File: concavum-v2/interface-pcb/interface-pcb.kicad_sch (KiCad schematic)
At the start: 6 parts, among them J1 Audio_Jack, J2 FPC_connector, U1 Adafruit_KB2040

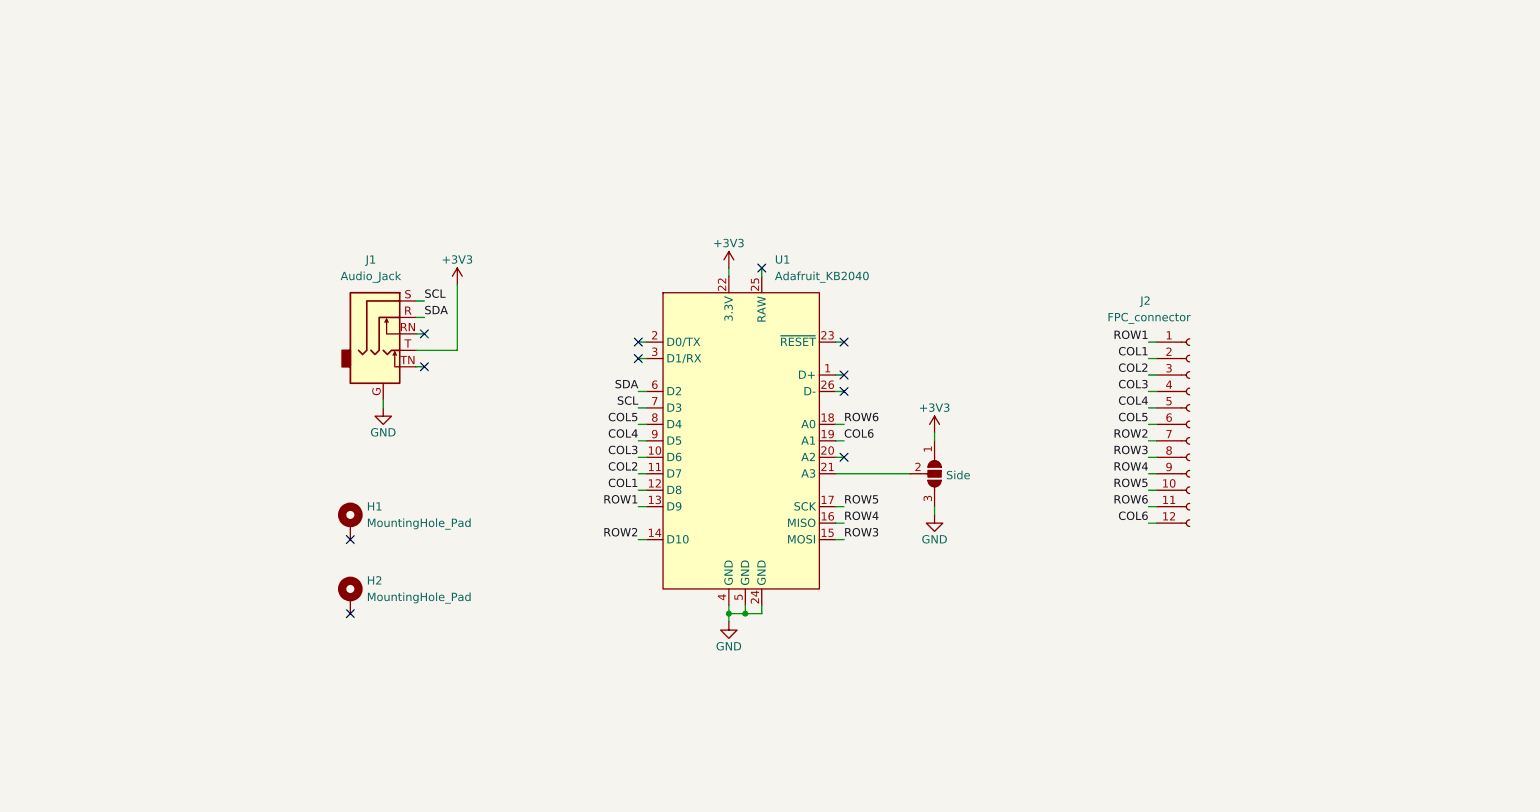
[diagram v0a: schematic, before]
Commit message: Implement VBUS detection and make PCB symmetric
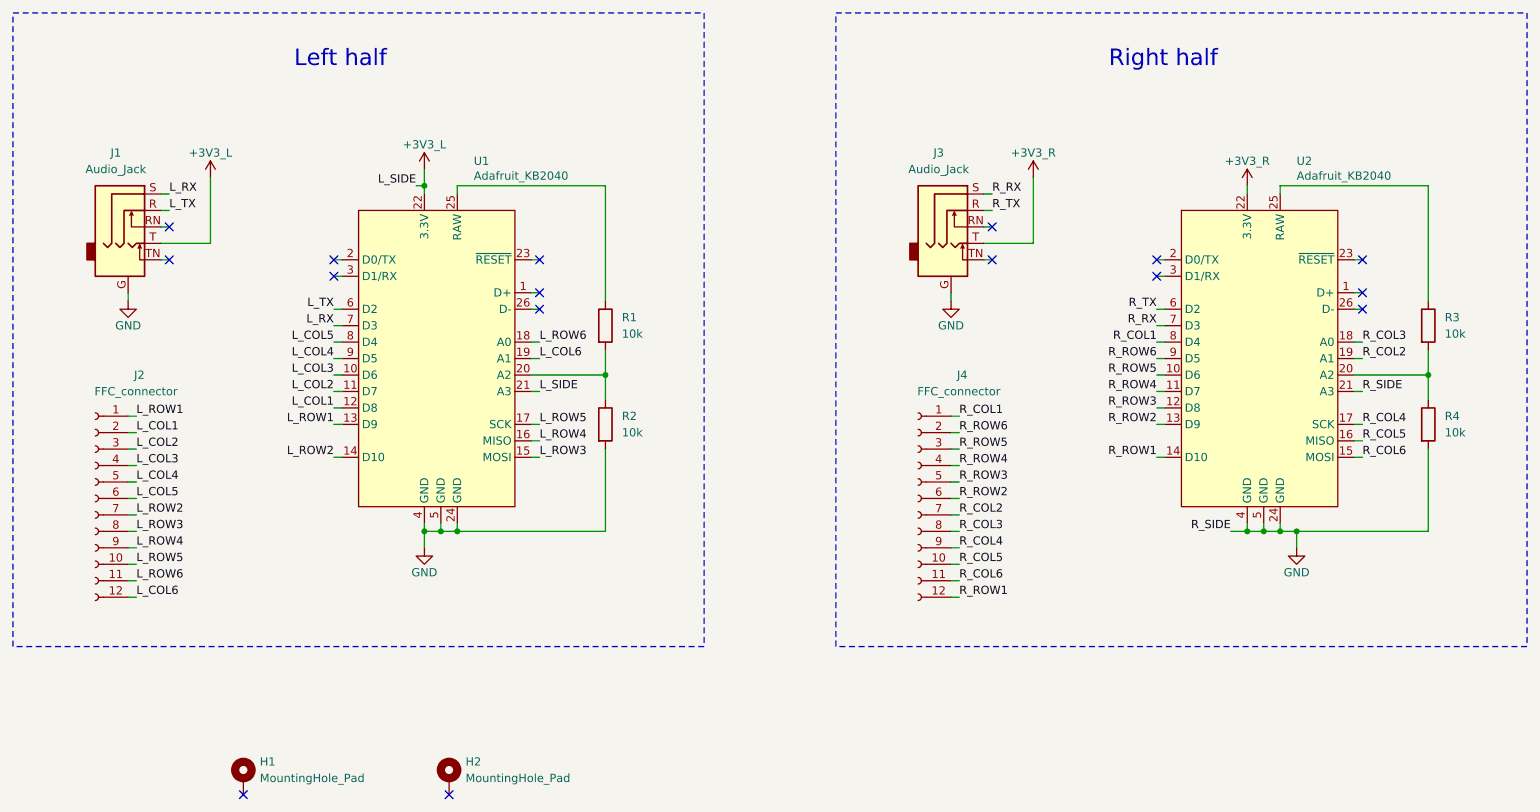
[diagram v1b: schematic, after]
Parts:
- removed JP1: Side, Jumper:SolderJumper-3_P1.3mm_Open_RoundedPad1.0x1.5mm, symbol Jumper:SolderJumper_3_Open
- added J3: Audio_Jack, Custom:Audio_Jack, symbol Connector:AudioJack3_Ground_SwitchTR
- added J4: FFC_connector, Custom:FPC_Connector, symbol Connector:Conn_01x12_Female
- added R1, R2, R3, R4: 10k, Resistor_SMD:R_1206_3216Metric, symbol Device:R
- added U2: Adafruit_KB2040, Custom:Adafruit_KB2040, symbol Custom:Adafruit_KB2040
- J2: value FPC_connector -> FFC_connector
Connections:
- net +3V3 is gone; now on net +3V3_L: J1.T, U1.22 (3.3V)
- net GND: now also J3.G, R2.2, R4.2, U2.21 (A3), U2.24 (GND), U2.4 (GND), U2.5 (GND)
- net +3V3_L: now reaches U1.21 (A3)
- net at U1.20 (A2): now also R1.2, R2.1
- net at U1.25 (RAW): now also R1.1
- net COL1 renamed L_COL1
- net COL2 renamed L_COL2
- net COL3 renamed L_COL3
- net COL4 renamed L_COL4
- net COL5 renamed L_COL5
- net COL6 renamed L_COL6
- net ROW1 renamed L_ROW1
- net ROW2 renamed L_ROW2
- net ROW3 renamed L_ROW3
- net ROW4 renamed L_ROW4
- net ROW5 renamed L_ROW5
- net ROW6 renamed L_ROW6
- net SCL renamed L_RX
- net SDA renamed L_TX
- new net: R3.2, R4.1, U2.20 (A2)
- new net: R3.1, U2.25 (RAW)
- new net +3V3_R: J3.T, U2.22 (3.3V)
- new net R_COL1: J4.1 (Pin_1), U2.8 (D4)
- new net R_COL2: J4.7 (Pin_7), U2.19 (A1)
- new net R_COL3: J4.8 (Pin_8), U2.18 (A0)
- new net R_COL4: J4.9 (Pin_9), U2.17 (SCK)
- new net R_COL5: J4.10 (Pin_10), U2.16 (MISO)
- new net R_COL6: J4.11 (Pin_11), U2.15 (MOSI)
- new net R_ROW1: J4.12 (Pin_12), U2.14 (D10)
- new net R_ROW2: J4.6 (Pin_6), U2.13 (D9)
- new net R_ROW3: J4.5 (Pin_5), U2.12 (D8)
- new net R_ROW4: J4.4 (Pin_4), U2.11 (D7)
- new net R_ROW5: J4.3 (Pin_3), U2.10 (D6)
- new net R_ROW6: J4.2 (Pin_2), U2.9 (D5)
- new net R_RX: J3.S, U2.7 (D3)
- new net R_TX: J3.R, U2.6 (D2)
- no-connect marks 11 -> 16
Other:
- note added: "Left half"
- note added: "Right half"
- moved on the sheet: H1, H2, J1, J2, U1

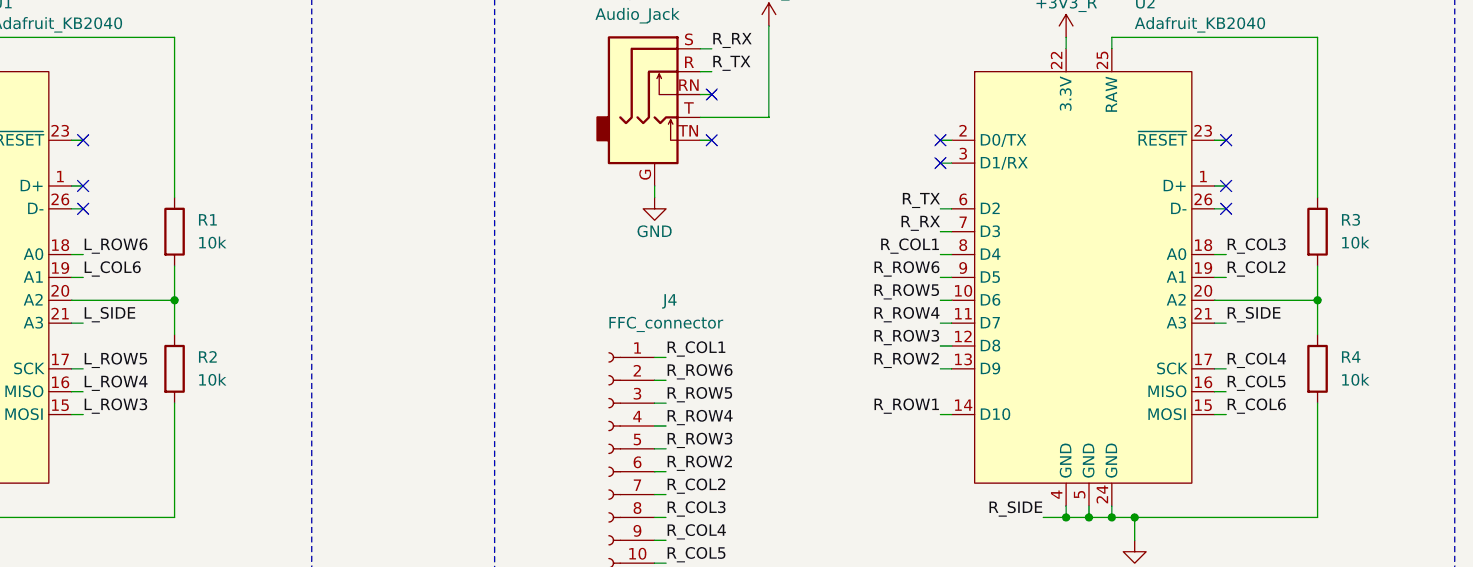
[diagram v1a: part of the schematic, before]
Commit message: Use a zener diode for VBUS detection circuit
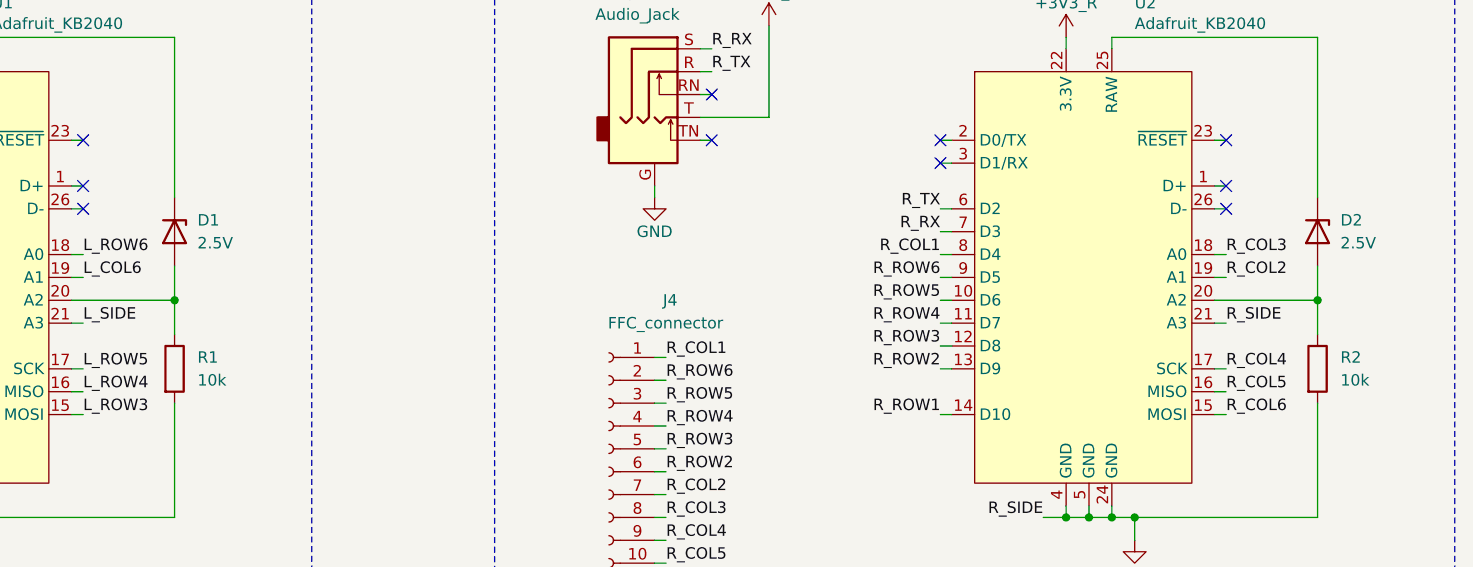
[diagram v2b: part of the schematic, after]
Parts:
- removed R1, R3: 10k, Resistor_SMD:R_1206_3216Metric, symbol Device:R
- added D1, D2: 2.5V, Diode_SMD:D_MiniMELF, symbol Device:D_Zener
- renumbered R2 to R1, R4 to R2
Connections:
- net at R1.1, U1.20 (A2): now also D1.2 (A)
- net at U1.25 (RAW): now also D1.1 (K)
- net at R2.1, U2.20 (A2): now also D2.2 (A)
- net at U2.25 (RAW): now also D2.1 (K)
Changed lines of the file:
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@@
 		(dnp no)
 		(fields_autoplaced yes)
-		(property "Reference" "R2"
+		(property "Reference" "R1"
 			(at 125.73 93.9799 0)
 			(effects
@@
 			(project "interface-pcb"
 				(path "/9538e4ed-27e6-4c37-b989-9859dc0d49e8"
-					(reference "R2")
+					(reference "R1")
 					(unit 1)
 				)
@@
 	)
 	(symbol
+		(lib_id "Device:D_Zener")
+		(at 123.19 80.01 270)
+		(unit 1)
+		(exclude_from_sim no)
+		(in_bom yes)
+		(on_board yes)
+		(dnp no)
+		(fields_autoplaced yes)
+		(property "Reference" "D1"
+			(at 125.73 78.7399 90)
+			(effects
+				(font
+					(size 1.27 1.27)
+				)
+				(justify left)
+			)
+		)
+		(property "Value" "2.5V"
+			(at 125.73 81.2799 90)
+			(effects
+				(font
+					(size 1.27 1.27)
+				)
+				(justify left)
+			)
+		)
+		(property "Footprint" "Diode_SMD:D_MiniMELF"
+			(at 123.19 80.01 0)
+			(effects
+				(font
+					(size 1.27 1.27)
+				)
+				(hide yes)
+			)
+		)
+		(property "Datasheet" "~"
+			(at 123.19 80.01 0)
+			(effects
+				(font
+					(size 1.27 1.27)
+				)
+				(hide yes)
+			)
+		)
+		(property "Description" "Zener diode"
+			(at 123.19 80.01 0)
+			(effects
+				(font
+					(size 1.27 1.27)
+				)
+				(hide yes)
+			)
+		)
+		(pin "1"
+		)
+		(pin "2"
+		)
+		(instances
+			(project ""
+				(path "/9538e4ed-27e6-4c37-b989-9859dc0d49e8"
+					(reference "D1")
+					(unit 1)
+				)
+			)
+		)
+	)
+	(symbol
 		(lib_id "power:+3.3V")
 		(at 222.25 58.42 0)
@@
 				(path "/9538e4ed-27e6-4c37-b989-9859dc0d49e8"
 					(reference "#PWR06")
-					(unit 1)
-				)
-			)
-		)
-	)
-	(symbol
-		(lib_id "Device:R")
-		(at 123.19 80.01 0)
-		(unit 1)
-		(exclude_from_sim no)
-		(in_bom yes)
-		(on_board yes)
-		(dnp no)
-		(fields_autoplaced yes)
-		(property "Reference" "R1"
-			(at 125.73 78.7399 0)
-			(effects
-				(font
-					(size 1.27 1.27)
-				)
-				(justify left)
-			)
-		)
-		(property "Value" "10k"
-			(at 125.73 81.2799 0)
-			(effects
-				(font
-					(size 1.27 1.27)
-				)
-				(justify left)
-			)
-		)
-		(property "Footprint" "Resistor_SMD:R_1206_3216Metric"
-			(at 121.412 80.01 90)
-			(effects
-				(font
-					(size 1.27 1.27)
-				)
-				(hide yes)
-			)
-		)
-		(property "Datasheet" "~"
-			(at 123.19 80.01 0)
-			(effects
-				(font
-					(size 1.27 1.27)
-				)
-				(hide yes)
-			)
-		)
-		(property "Description" "Resistor"
-			(at 123.19 80.01 0)
-			(effects
-				(font
-					(size 1.27 1.27)
-				)
-				(hide yes)
-			)
-		)
-		(pin "1"
-		)
-		(pin "2"
-		)
-		(instances
-			(project ""
-				(path "/9538e4ed-27e6-4c37-b989-9859dc0d49e8"
-					(reference "R1")
 					(unit 1)
 				)
@@
 		(dnp no)
 		(fields_autoplaced yes)
-		(property "Reference" "R4"
+		(property "Reference" "R2"
 			(at 252.73 93.9799 0)
 			(effects
@@
 			(project "interface-pcb"
 				(path "/9538e4ed-27e6-4c37-b989-9859dc0d49e8"
-					(reference "R4")
+					(reference "R2")
 					(unit 1)
 				)
@@
 	)
 	(symbol
-		(lib_id "Device:R")
-		(at 250.19 80.01 0)
+		(lib_id "Device:D_Zener")
+		(at 250.19 80.01 270)
 		(unit 1)
 		(exclude_from_sim no)
@@
 		(dnp no)
 		(fields_autoplaced yes)
-		(property "Reference" "R3"
-			(at 252.73 78.7399 0)
-			(effects
-				(font
-					(size 1.27 1.27)
-				)
-				(justify left)
-			)
-		)
-		(property "Value" "10k"
-			(at 252.73 81.2799 0)
-			(effects
-				(font
-					(size 1.27 1.27)
-				)
-				(justify left)
-			)
-		)
-		(property "Footprint" "Resistor_SMD:R_1206_3216Metric"
-			(at 248.412 80.01 90)
+		(property "Reference" "D2"
+			(at 252.73 78.7399 90)
+			(effects
+				(font
+					(size 1.27 1.27)
+				)
+				(justify left)
+			)
+		)
+		(property "Value" "2.5V"
+			(at 252.73 81.2799 90)
+			(effects
+				(font
+					(size 1.27 1.27)
+				)
+				(justify left)
+			)
+		)
+		(property "Footprint" "Diode_SMD:D_MiniMELF"
+			(at 250.19 80.01 0)
 			(effects
 				(font
@@
 			)
 		)
-		(property "Description" "Resistor"
+		(property "Description" "Zener diode"
 			(at 250.19 80.01 0)
 			(effects
@@
 			(project "interface-pcb"
 				(path "/9538e4ed-27e6-4c37-b989-9859dc0d49e8"
-					(reference "R3")
-					(unit 1)
-				)
+					(reference "D2")
+					(unit 1)
+				)

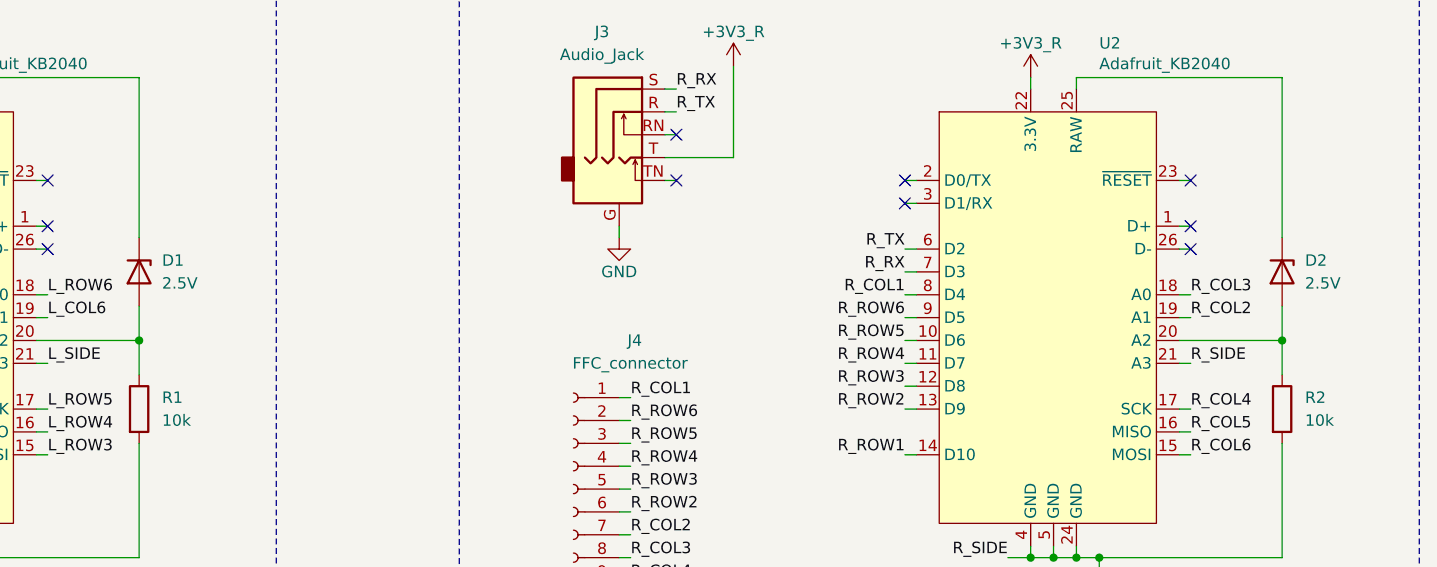
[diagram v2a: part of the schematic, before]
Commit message: Replace 2.5V zener diode with 3.6V one
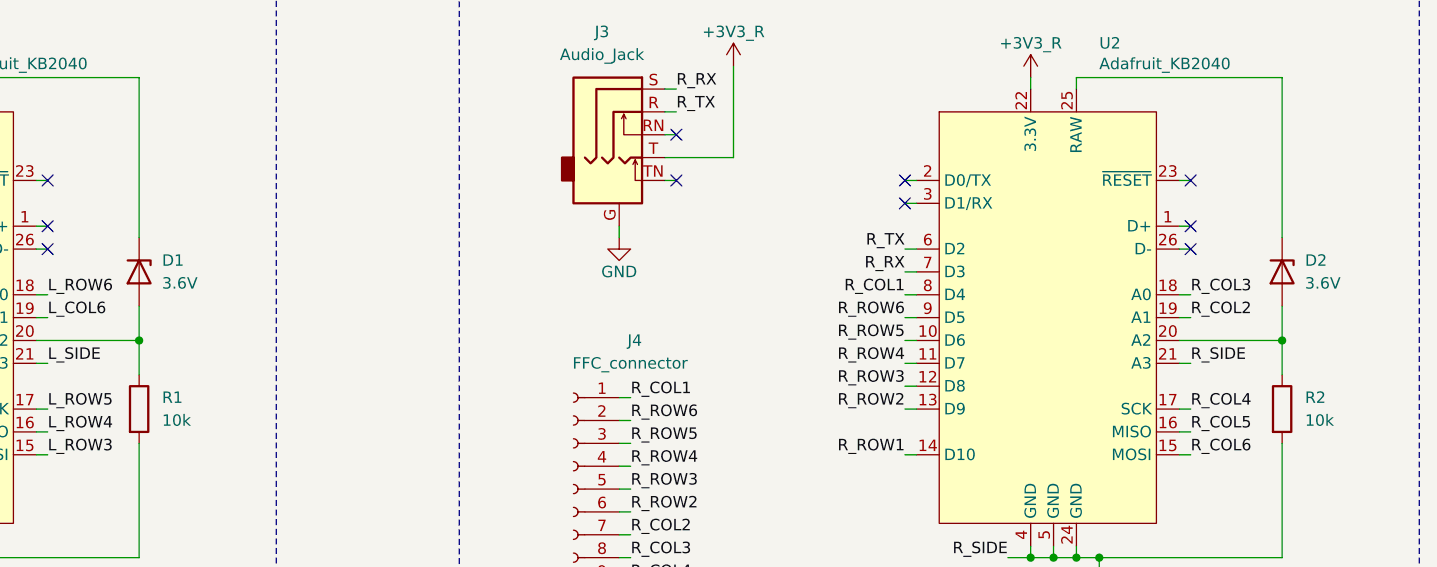
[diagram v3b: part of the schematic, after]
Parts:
- D1, D2: value 2.5V -> 3.6V
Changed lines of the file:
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@@
 			)
 		)
-		(property "Value" "2.5V"
+		(property "Value" "3.6V"
 			(at 125.73 81.2799 90)
 			(effects
@@
 			)
 		)
-		(property "Value" "2.5V"
+		(property "Value" "3.6V"
 			(at 252.73 81.2799 90)
 			(effects
